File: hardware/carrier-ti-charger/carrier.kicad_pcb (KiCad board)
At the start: 4 copper layers, 105 x 95 mm, 184 parts, among them J1 MC-107DMS, J10 J_ADS_MAIN ADSBee J5, J11 J_ADS_GNSS ADSBee J4, J12 CONTROLS, J2 J_NTC 100k ENTC-EB-100K4262-02, J3 J_BAT JST-PH 2mm, J4 J_THERM 60C NC, J5 J_GNSS GPS-18037 J5, J6 J_ESP_A support, J7 J_ESP_B power/UART, J8 J_ESP_C I2C, J9 J_ESP_D support, Q10 2N7002, Q11 2N7002, Q12 2N7002, Q13 CSD17575Q3, Q2 AO3401A, Q3 AO3401A, Q4 AO3401A, Q7 AO3401A, Q8 2N7002, Q9 2N7002, SW1 K3-1280S-F1, SW2 K3-1280S-F1, SW3 K3-1280S-F1, SW4 RESET 6x6, U10 BMP580, U11 TPS259474LRPWR, U12 TPS259474LRPWR, U13 TCA9534PWR, U14 TPS259474LRPWR, U4 BQ25798RQMR, U5 TLV840CADL29DBVR 2.9V, U6 TPS61088RHLR, U7 TPS22975DSGR, U8 MAX17048G+T10, U9 SN74LVC1G17DBVR

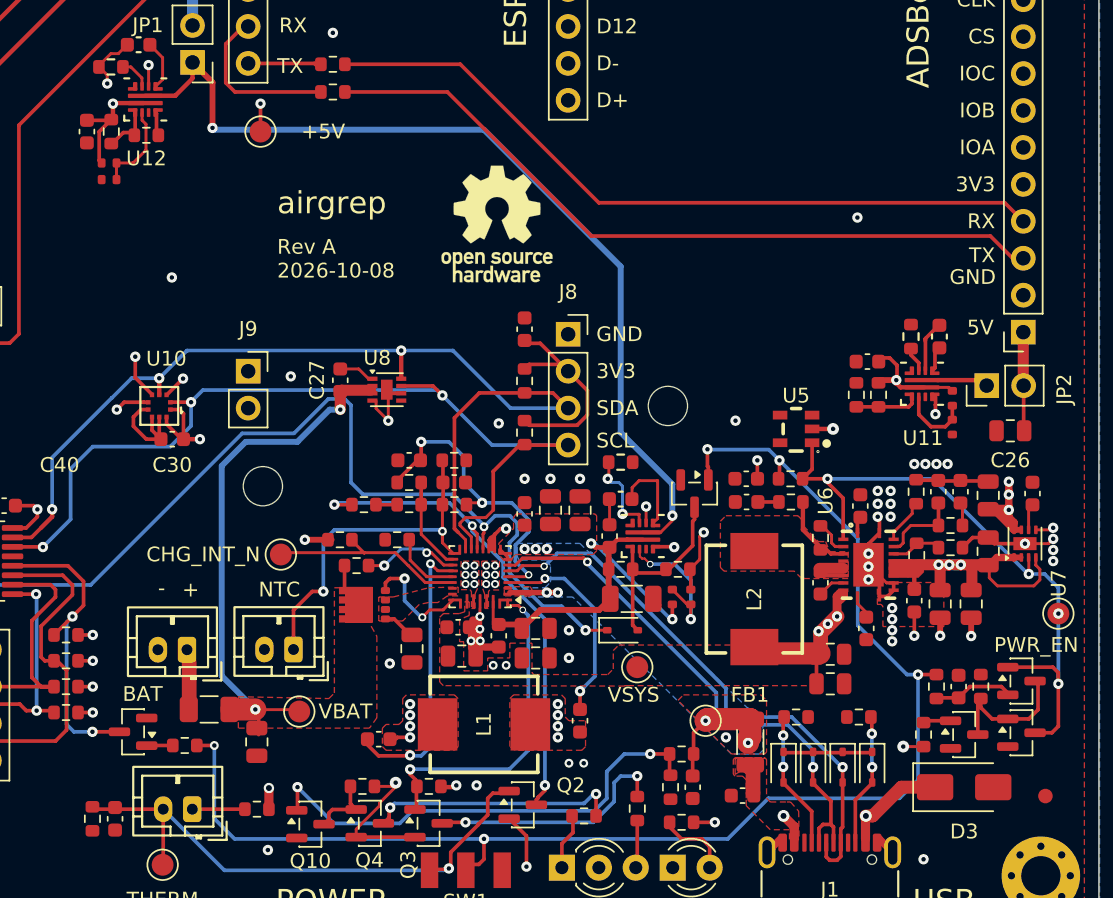
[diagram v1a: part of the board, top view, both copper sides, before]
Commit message: Update resistors for stock availability.
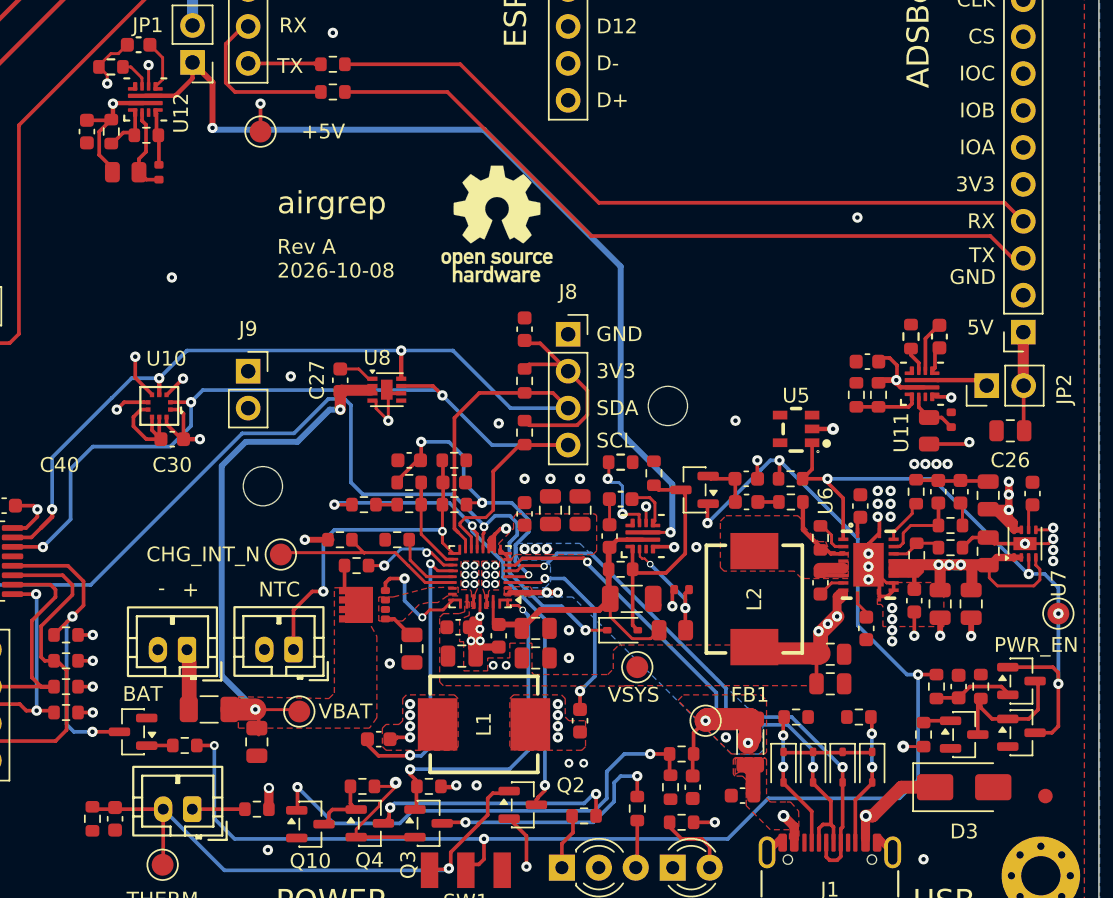
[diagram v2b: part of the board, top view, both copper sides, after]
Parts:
- R73, R75, R77: value 5.1k -> 5.36k; footprint carrier:R_0402_1005Metric_NoSilk -> carrier:R_0805_2012Metric_NoSilk
- moved R68 6.81 mm to (125.7, 102.4), turned to 90 degrees
- moved R76 3.47 mm to (91.7, 81.7), turned to 90 degrees
- moved R73 2.75 mm to (144.7, 99.4), turned to 90 degrees
- moved R77 2.29 mm to (127.0, 113.2), turned to 0 degrees
- moved R75 1.31 mm to (89.4, 81.7)
- moved R78 0.81 mm to (127.6, 110.4), turned to 180 degrees
- moved R74 0.51 mm to (146.2, 98.7), turned to 90 degrees
- moved Q12 0.25 mm to (128.5, 103.5), turned to 180 degrees
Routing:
- net CHG_PMID: track 26.6 -> 21.7 mm, vias 2 -> 0
- net /Charger BQ25798/ESP_PMID_EN: track 13.0 -> 16.4 mm
- net U14_DVDT: track 5.79 -> 3.07 mm
- net U14_OVLO: track 10.3 -> 8.33 mm
- net GND: track 113.8 -> 115.7 mm, vias 69 -> 70
- net U11_OVLO: track 5.03 -> 3.51 mm
- net CHG_INT_N: track 14.2 -> 13.4 mm
- net +5V: track 152.0 -> 152.8 mm, vias 7 -> 8
- net +ESP_5V_D: track 62.9 -> 63.6 mm
- net SW_EN: track 95.7 -> 96.3 mm
- net THERM_OK: track 39.0 -> 38.4 mm

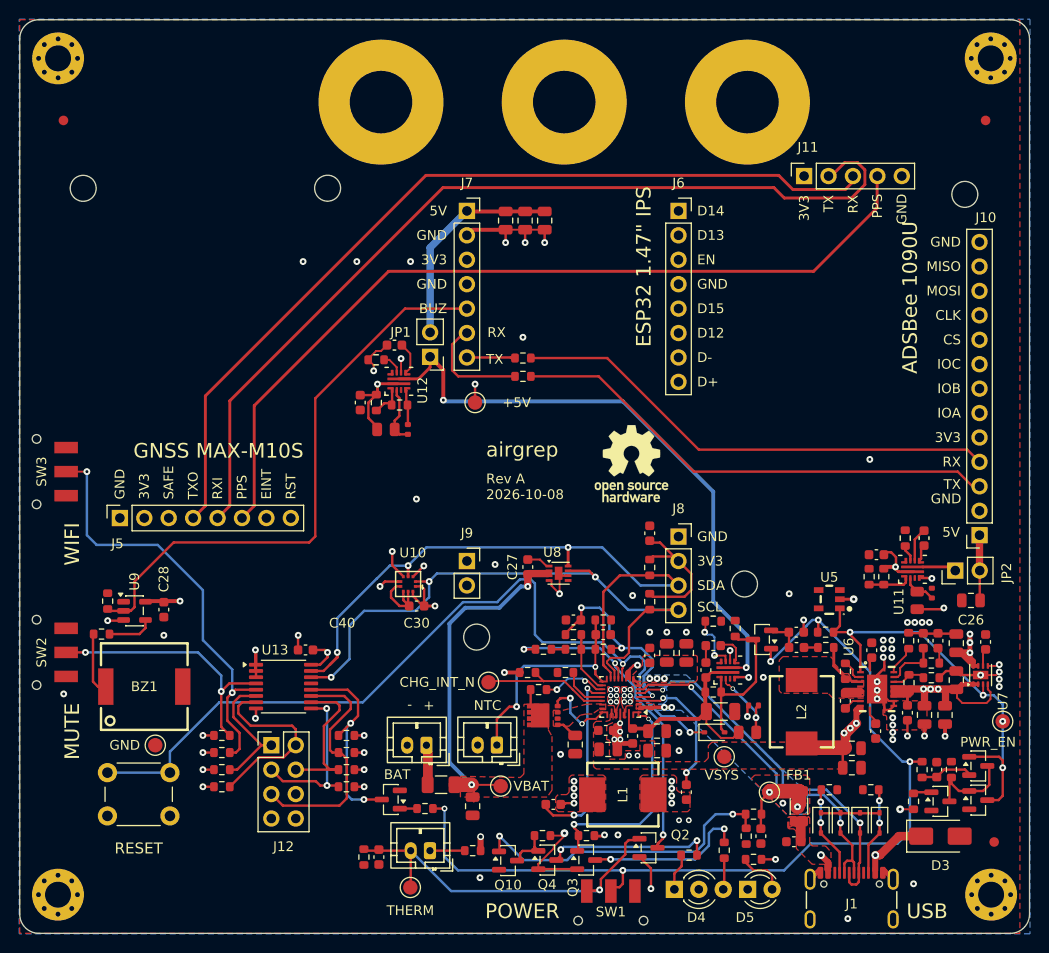
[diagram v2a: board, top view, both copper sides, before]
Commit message: Add USB current detection.
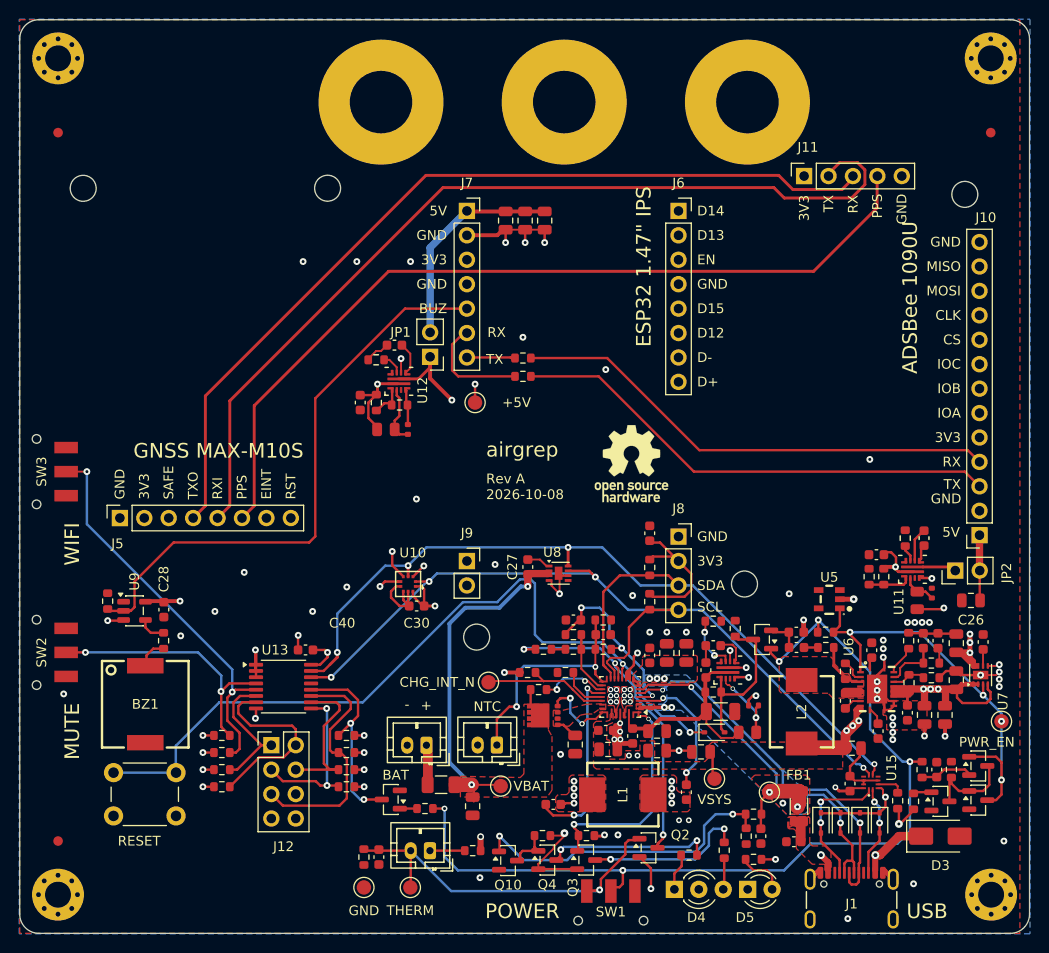
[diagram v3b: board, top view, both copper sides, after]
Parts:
- removed R65, R66: 5.1k 1%, Resistor_SMD:R_0603_1608Metric
- added C57: 100n 50V, Capacitor_SMD:C_0603_1608Metric, F.Cu at (137.7, 118.5)
- added R79: 887k 1%, Resistor_SMD:R_0603_1608Metric, F.Cu at (142.6, 120.3)
- added U15: TUSB320LIRWBR, carrier:X2QFN-12_L1.6-W1.6-P0.40-TL, F.Cu at (139.8, 118.4)
- J2: value J_NTC 100k ENTC-EB-100K4262-02 -> NTC
- J3: value J_BAT JST-PH 2mm -> BAT
- J4: value J_THERM 60C NC -> THERM
- R57: value 47k 1% -> 120k 1%
- moved FID3 97.3 mm to (55.3, 124.5)
- moved TP6 26.3 mm to (87.1, 129.3)
- moved C14 15.8 mm to (122.2, 115.2), turned to 180 degrees
- moved R28 6.49 mm to (66.3, 103.6), turned to -90 degrees
- moved TP2 2.50 mm to (123.6, 118.0)
- moved BZ1 1.84 mm to (64.4, 110.2), turned to -90 degrees
- moved FID1 1.39 mm to (55.3, 50.8)
- moved FID2 1.38 mm to (152.3, 50.8)
- moved SW4 0.64 mm to (61.1, 117.3)
- moved C17 0.25 mm to (140.6, 113.0)
- moved C23 0.25 mm to (151.5, 103.8)
- moved TP3 0.13 mm to (153.4, 112.0)
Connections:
- net ADS_ID_EN renamed /Modules and service shunts/ADS_ID_EN
- net ESP_ID_EN renamed /Modules and service shunts/ESP_ID_EN
- net U11_DVDT renamed /Modules and service shunts/U11_DVDT
- net U11_ILM renamed /Modules and service shunts/U11_ILM
- net U11_OVLO renamed /Modules and service shunts/U11_OVLO
- net U12_DVDT renamed /Modules and service shunts/U12_DVDT
- net U12_ILM renamed /Modules and service shunts/U12_ILM
- net U12_OVLO renamed /Modules and service shunts/U12_OVLO
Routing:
- net +ESP_3V3: track 209.2 -> 246.4 mm, vias 13 -> 14
- net I2C_SDA: track 69.0 -> 98.6 mm, vias 3 -> 4
- net I2C_SCL: track 65.0 -> 89.0 mm, vias 3 -> 4
- net GND: track 115.7 -> 126.6 mm, vias 70 -> 71
- net USB_CC1: track 9.18 -> 13.6 mm
- net +ESP_5V_D: track 63.6 -> 59.5 mm
- net BUZZ_LIM: track 6.43 -> 2.64 mm
- net WIFI_ENABLE: track 45.5 -> 41.7 mm
- net +VUSB: track 26.5 -> 29.7 mm
- net U15_VBUS_DET: track 0.00 -> 2.82 mm
- net CHG_QON_N: track 86.5 -> 83.7 mm
- net CHG_REGN: track 21.2 -> 19.3 mm
- net BUZZ_DRV: track 4.71 -> 2.89 mm
- net +VSYS: track 92.2 -> 93.4 mm
- net +5V: track 152.8 -> 151.8 mm
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
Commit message: Switch to faster FUSB303B USB controller.
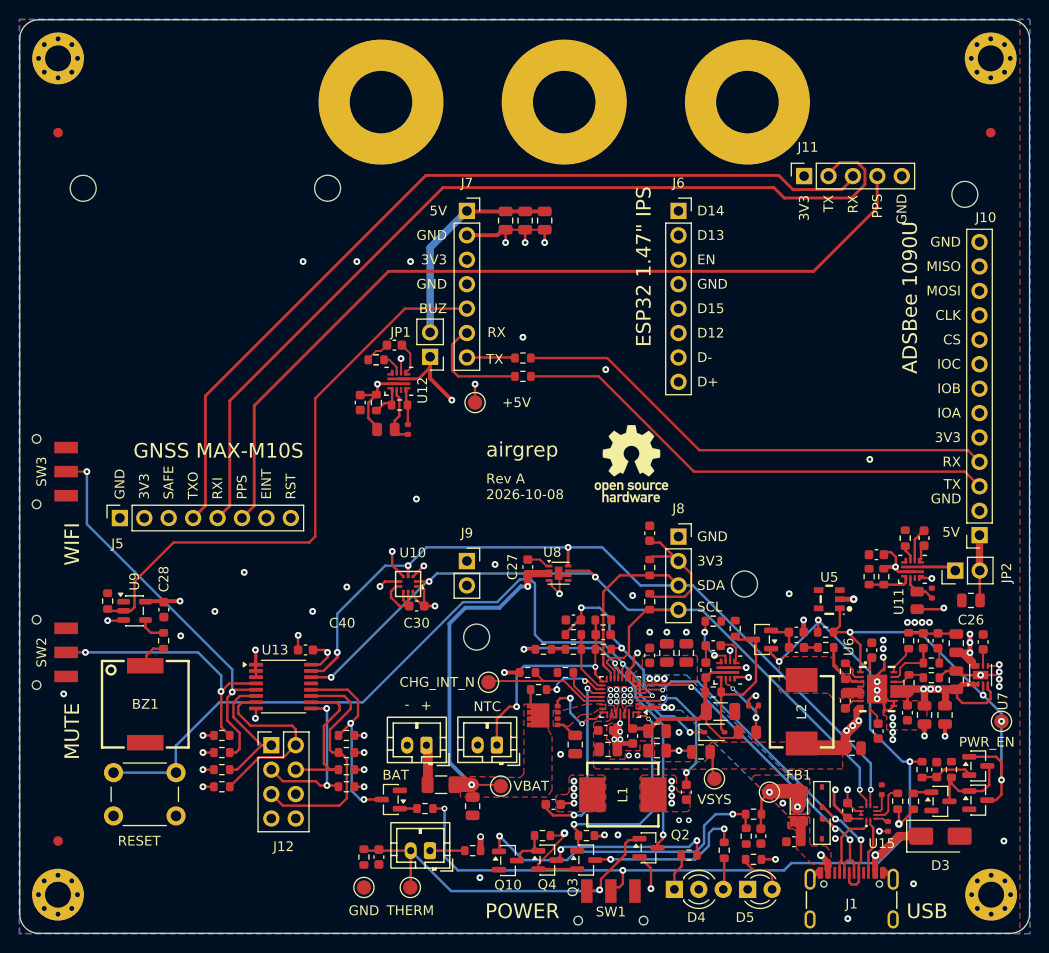
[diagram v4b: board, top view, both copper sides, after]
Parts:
- removed D6, D7: H5VLD3B ESD 5V, Diode_SMD:D_SOD-323
- added R80: 910k 1%, carrier:R_0402_1005Metric_NoSilk, F.Cu at (141.6, 122.9)
- added R81: 910k 1%, carrier:R_0402_1005Metric_NoSilk, F.Cu at (141.0, 119.1)
- R19, R20: value 2.2k -> 1.8k
- U15: value TUSB320LIRWBR -> FUSB303BTMX
- moved D8 4.79 mm to (134.7, 119.9)
- moved U15 3.19 mm to (139.6, 121.5)
- moved C57 2.81 mm to (137.4, 121.3)
- moved D9 2.02 mm to (134.7, 123.2), turned to 90 degrees
- moved R79 0.05 mm to (142.6, 120.3)
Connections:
- net U15_VBUS_DET renamed VBUS_DET
- U15 pad 3: GND -> PORT
- U15 pad 5: GND -> ADDR
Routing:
- net GND: track 126.6 -> 115.1 mm, vias 71 -> 73
- net USB_CC1: track 13.6 -> 7.20 mm, vias 2 -> 0
- net USB_CC2: track 9.07 -> 5.56 mm, vias 2 -> 0
- net I2C_SCL: track 89.0 -> 91.9 mm
- net I2C_SDA: track 98.6 -> 101.4 mm
- net +ESP_3V3: track 246.4 -> 248.7 mm
- net ADDR: track 0.00 -> 2.24 mm
- net PORT: track 0.00 -> 1.40 mm
- net VBUS_DET: track 2.82 -> 4.22 mm
- net +VUSB: track 29.7 -> 30.3 mm
- net GNSS_RXI: track 95.1 -> 94.6 mm
- net USB_D-: track 35.8 -> 35.6 mm, vias 2 -> 3
- net USB_D+: track 38.7 -> 38.8 mm, vias 2 -> 3

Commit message: Refine resistors.
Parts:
- L1: value 2.2uH FXL0630-2R2-M -> 2.2uH FC-ALX4030D-2R2MT; footprint carrier:IND-SMD_L7.0-W6.6_FXL0630 -> carrier:IND-SMD_L4.2-W4.2_FC-ALX4030D
- L2: value 2.2uH CKST0603 -> 2.2uH FC-ALX4030D-2R2MT; footprint carrier:IND-SMD_L7.4-W6.6 -> carrier:IND-SMD_L4.2-W4.2_FC-ALX4030D
- R73, R75, R77: footprint carrier:R_0805_2012Metric_NoSilk -> Resistor_SMD:R_0603_1608Metric
- moved R67 5.40 mm to (128.4, 106.8), turned to 90 degrees
- moved R77 3.90 mm to (128.3, 109.5), turned to 180 degrees
- moved C45 3.87 mm to (109.3, 117.7), turned to -90 degrees
- moved C33 3.49 mm to (127.6, 111.6), turned to 180 degrees
- moved C8 2.34 mm to (118.4, 118.9)
- moved D10 2.09 mm to (124.1, 111.1), turned to 90 degrees
- moved R78 2.03 mm to (125.8, 109.5), turned to -90 degrees
- moved L2 1.44 mm to (133.2, 109.7)
- moved R74 0.40 mm to (146.6, 98.8), turned to 0 degrees
- moved R75 0.38 mm to (89.4, 81.3)
- moved C44 0.25 mm to (115.1, 113.8)
- moved R76 0.25 mm to (91.7, 81.4)
- moved C10 0.13 mm to (117.6, 115.2)
- moved C6 0.13 mm to (117.6, 113.2)
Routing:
- net +ESP_3V3: track 248.7 -> 267.7 mm
- net +VSYS: track 93.4 -> 86.3 mm
- net CHG_BTST2: track 19.3 -> 12.7 mm
- net U14_OVLO: track 8.33 -> 3.73 mm, vias 2 -> 0
- net +ESP_5V_D: track 59.5 -> 63.6 mm
- net GND: track 115.1 -> 118.0 mm
- net CHG_STAT_N: track 22.6 -> 20.6 mm
- net CHG_BTST1: track 13.8 -> 15.6 mm
- net CHG_SDRV: track 7.79 -> 6.49 mm
- net I2C_SDA: track 101.4 -> 102.6 mm
- net CHG_SW1: track 0.00 -> 1.21 mm
- net CHG_QON_N: track 83.7 -> 84.9 mm
- net /Charger BQ25798/ESP_PMID_EN: track 16.4 -> 17.6 mm, vias 0 -> 2
- net CHG_PMID: track 21.7 -> 22.3 mm
- net I2C_SCL: track 91.9 -> 92.4 mm
